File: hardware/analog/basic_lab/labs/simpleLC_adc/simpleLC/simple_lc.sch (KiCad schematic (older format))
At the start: 10 parts, among them J1 Conn_01x04_Male, Q1 FQP27P06, Q2 BC547

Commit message: Simple lc => adc v1, jlcpcb order
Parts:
- removed C2: C, Capacitor_THT:C_Axial_L12.0mm_D6.5mm_P15.00mm_Horizontal, symbol Device:C
- removed L1: L, Inductor_THT:L_Axial_L5.3mm_D2.2mm_P2.54mm_Vertical_Vishay_IM-1, symbol Device:L
- removed Q1: FQP27P06, Package_TO_SOT_THT:TO-220-3_Vertical, symbol Transistor_FET:FQP27P06
- removed R1, R2, R3: R, Resistor_THT:R_Axial_DIN0207_L6.3mm_D2.5mm_P2.54mm_Vertical, symbol Device:R
- added J2: Conn_01x02_Male, Connector_PinHeader_2.54mm:PinHeader_1x02_P2.54mm_Vertical, symbol Connector:Conn_01x02_Male
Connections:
- net labels removed: din
- wire segments 28 -> 19
- no-connect marks 0 -> 1
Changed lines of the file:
@@
 Comment4 ""
 $EndDescr
-Text GLabel 2250 2900 0    50   Input ~ 0
-din
-$Comp
-L power:+3.3V #PWR0101
-U 1 1 60C11C18
-P 3250 2000
-F 0 "#PWR0101" H 3250 1850 50  0001 C CNN
-F 1 "+3.3V" H 3265 2173 50  0000 C CNN
-F 2 "" H 3250 2000 50  0001 C CNN
-F 3 "" H 3250 2000 50  0001 C CNN
-	1    3250 2000
-	1    0    0    -1
-$EndComp
-$Comp
-L power:GND #PWR0102
-U 1 1 60C11E84
-P 3250 3650
-F 0 "#PWR0102" H 3250 3400 50  0001 C CNN
-F 1 "GND" H 3255 3477 50  0000 C CNN
-F 2 "" H 3250 3650 50  0001 C CNN
-F 3 "" H 3250 3650 50  0001 C CNN
-	1    3250 3650
-	1    0    0    -1
-$EndComp
-$Comp
-L Transistor_FET:FQP27P06 Q1
-U 1 1 60C127AE
-P 3150 2900
-F 0 "Q1" H 3354 2946 50  0000 L CNN
-F 1 "FQP27P06" H 3354 2855 50  0000 L CNN
-F 2 "Package_TO_SOT_THT:TO-220-3_Vertical" H 3350 2825 50  0001 L CIN
-F 3 "https://www.onsemi.com/pub/Collateral/FQP27P06-D.PDF" H 3150 2900 50  0001 L CNN
-	1    3150 2900
-	1    0    0    -1
-$EndComp
-$Comp
-L Device:R R1
-U 1 1 60C12EAB
-P 3250 2300
-F 0 "R1" H 3320 2346 50  0000 L CNN
-F 1 "R" H 3320 2255 50  0000 L CNN
-F 2 "Resistor_THT:R_Axial_DIN0207_L6.3mm_D2.5mm_P2.54mm_Vertical" V 3180 2300 50  0001 C CNN
-F 3 "~" H 3250 2300 50  0001 C CNN
-	1    3250 2300
-	1    0    0    -1
-$EndComp
-Wire Wire Line
-	3250 2000 3250 2150
-Wire Wire Line
-	3250 2450 3250 2550
-Wire Wire Line
-	3250 3100 3250 3200
-Wire Wire Line
-	2250 2900 2950 2900
-Wire Wire Line
-	3250 3500 3250 3650
-$Comp
-L Device:L L1
-U 1 1 60C1394D
-P 4400 2800
-F 0 "L1" H 4453 2846 50  0000 L CNN
-F 1 "L" H 4453 2755 50  0000 L CNN
-F 2 "Inductor_THT:L_Axial_L5.3mm_D2.2mm_P2.54mm_Vertical_Vishay_IM-1" H 4400 2800 50  0001 C CNN
-F 3 "~" H 4400 2800 50  0001 C CNN
-	1    4400 2800
-	1    0    0    -1
-$EndComp
-$Comp
-L power:GND #PWR0103
-U 1 1 60C13B88
-P 4400 3100
-F 0 "#PWR0103" H 4400 2850 50  0001 C CNN
-F 1 "GND" H 4405 2927 50  0000 C CNN
-F 2 "" H 4400 3100 50  0001 C CNN
-F 3 "" H 4400 3100 50  0001 C CNN
-	1    4400 3100
-	1    0    0    -1
-$EndComp
-Wire Wire Line
-	4400 2950 4400 3100
-Wire Wire Line
-	4400 2550 4400 2650
 $Comp
 L Device:C C1
@@
 	1    0    0    -1
 $EndComp
-Wire Wire Line
-	4400 2550 5100 2550
 Wire Wire Line
 	5100 2550 5100 2650
@@
 Wire Wire Line
 	5100 2950 5100 3150
-$Comp
-L Device:R R3
-U 1 1 60C14E91
-P 5650 2550
-F 0 "R3" V 5443 2550 50  0000 C CNN
-F 1 "R" V 5534 2550 50  0000 C CNN
-F 2 "Resistor_THT:R_Axial_DIN0207_L6.3mm_D2.5mm_P2.54mm_Vertical" V 5580 2550 50  0001 C CNN
-F 3 "~" H 5650 2550 50  0001 C CNN
-	1    5650 2550
-	0    1    1    0
-$EndComp
 $Comp
 L Device:R R5
@@
 Wire Wire Line
 	6300 3500 6300 3650
-Wire Wire Line
-	5100 2550 5500 2550
-Connection ~ 5100 2550
 $Comp
 L power:+3.3V #PWR0106
@@
 Wire Wire Line
 	10000 1650 10000 1450
-Text GLabel 9350 1750 2    50   Input ~ 0
-din
 Text GLabel 9350 1850 2    50   Input ~ 0
 aout
@@
 Wire Wire Line
 	6300 2850 6300 3200
-Wire Wire Line
-	5800 2550 6000 2550
 $Comp
-L Device:R R2
-U 1 1 60C12C69
-P 3250 3350
-F 0 "R2" H 3320 3396 50  0000 L CNN
-F 1 "R" H 3320 3305 50  0000 L CNN
-F 2 "Resistor_THT:R_Axial_DIN0207_L6.3mm_D2.5mm_P2.54mm_Vertical" V 3180 3350 50  0001 C CNN
-F 3 "~" H 3250 3350 50  0001 C CNN
-	1    3250 3350
+L Connector:Conn_01x02_Male J2
+U 1 1 60CB004D
+P 3850 2550
+F 0 "J2" H 3958 2731 50  0000 C CNN
+F 1 "Conn_01x02_Male" H 3958 2640 50  0000 C CNN
+F 2 "Connector_PinHeader_2.54mm:PinHeader_1x02_P2.54mm_Vertical" H 3850 2550 50  0001 C CNN
+F 3 "~" H 3850 2550 50  0001 C CNN
+	1    3850 2550
 	1    0    0    -1
 $EndComp
+Wire Wire Line
+	4050 2550 5100 2550
+Connection ~ 5100 2550
+Wire Wire Line
+	5100 2550 6000 2550
 $Comp
-L Device:C C2
-U 1 1 60C95A6B
-P 3850 2550
-F 0 "C2" V 3598 2550 50  0000 C CNN
-F 1 "C" V 3689 2550 50  0000 C CNN
-F 2 "Capacitor_THT:C_Axial_L12.0mm_D6.5mm_P15.00mm_Horizontal" H 3888 2400 50  0001 C CNN
-F 3 "~" H 3850 2550 50  0001 C CNN
-	1    3850 2550
-	0    1    1    0
+L power:GND #PWR03
+U 1 1 60CB1E67
+P 4400 3150
+F 0 "#PWR03" H 4400 2900 50  0001 C CNN
+F 1 "GND" H 4405 2977 50  0000 C CNN
+F 2 "" H 4400 3150 50  0001 C CNN
+F 3 "" H 4400 3150 50  0001 C CNN
+	1    4400 3150
+	1    0    0    -1
 $EndComp
 Wire Wire Line
-	3250 2550 3700 2550
-Connection ~ 3250 2550
+	4050 2650 4400 2650
 Wire Wire Line
-	3250 2550 3250 2700
-Wire Wire Line
-	4000 2550 4400 2550
-Connection ~ 4400 2550
+	4400 2650 4400 3150
+NoConn ~ 9350 1750
 $EndSCHEMATC

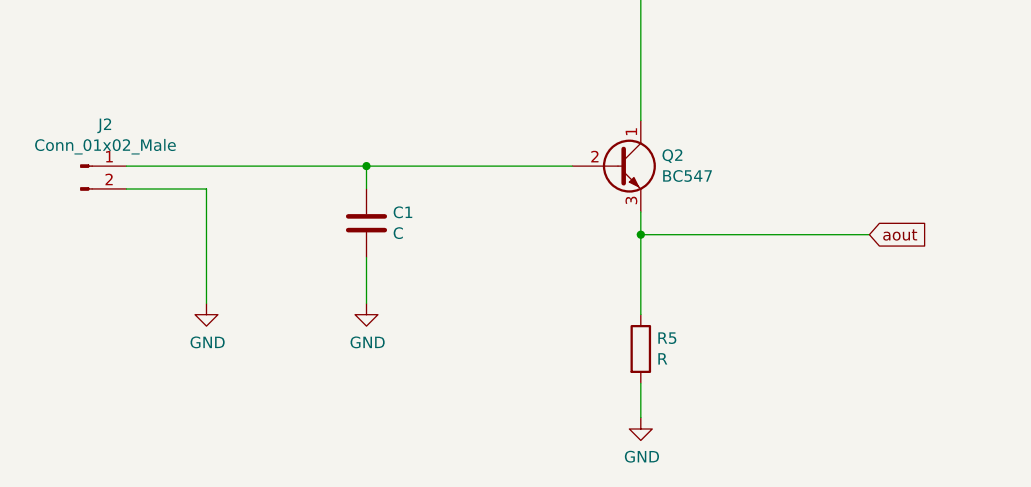
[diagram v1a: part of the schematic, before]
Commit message: pwm => adc: XFRM amplifier PCB
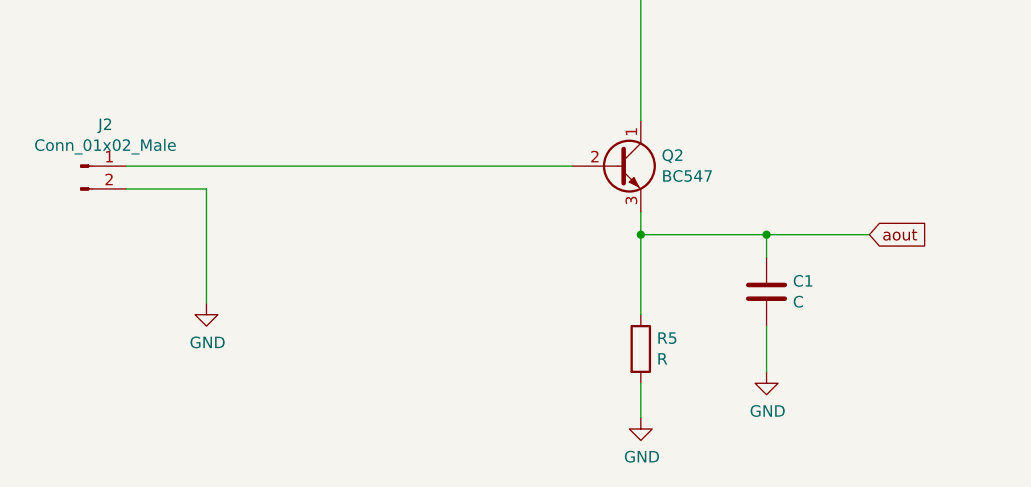
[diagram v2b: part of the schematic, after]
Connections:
- net aout: now also C1.1
- net at J2.1 (Pin_1), Q2.2 (B): no longer C1.1
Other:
- moved on the sheet: C1
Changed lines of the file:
@@
 L Device:C C1
 U 1 1 60C143B1
-P 5100 2800
-F 0 "C1" H 5215 2846 50  0000 L CNN
-F 1 "C" H 5215 2755 50  0000 L CNN
-F 2 "Capacitor_THT:C_Disc_D3.8mm_W2.6mm_P2.50mm" H 5138 2650 50  0001 C CNN
-F 3 "~" H 5100 2800 50  0001 C CNN
-	1    5100 2800
+P 6850 3100
+F 0 "C1" H 6965 3146 50  0000 L CNN
+F 1 "C" H 6965 3055 50  0000 L CNN
+F 2 "Capacitor_THT:C_Disc_D3.8mm_W2.6mm_P2.50mm" H 6888 2950 50  0001 C CNN
+F 3 "~" H 6850 3100 50  0001 C CNN
+	1    6850 3100
 	1    0    0    -1
 $EndComp
 Wire Wire Line
-	5100 2550 5100 2650
+	6850 2850 6850 2950
 $Comp
 L power:GND #PWR0104
 U 1 1 60C14856
-P 5100 3150
-F 0 "#PWR0104" H 5100 2900 50  0001 C CNN
-F 1 "GND" H 5105 2977 50  0000 C CNN
-F 2 "" H 5100 3150 50  0001 C CNN
-F 3 "" H 5100 3150 50  0001 C CNN
-	1    5100 3150
+P 6850 3450
+F 0 "#PWR0104" H 6850 3200 50  0001 C CNN
+F 1 "GND" H 6855 3277 50  0000 C CNN
+F 2 "" H 6850 3450 50  0001 C CNN
+F 3 "" H 6850 3450 50  0001 C CNN
+	1    6850 3450
 	1    0    0    -1
 $EndComp
 Wire Wire Line
-	5100 2950 5100 3150
+	6850 3250 6850 3450
 $Comp
 L Device:R R5
@@
 	6300 1650 6300 2350
 Wire Wire Line
-	6300 2850 7300 2850
+	6300 2850 6850 2850
 Connection ~ 6300 2850
 Wire Wire Line
@@
 	1    0    0    -1
 $EndComp
-Wire Wire Line
-	4050 2550 5100 2550
-Connection ~ 5100 2550
-Wire Wire Line
-	5100 2550 6000 2550
 $Comp
 L power:GND #PWR03
@@
 	4400 2650 4400 3150
 NoConn ~ 9350 1750
+Connection ~ 6850 2850
+Wire Wire Line
+	6850 2850 7300 2850
+Wire Wire Line
+	4050 2550 6000 2550
 $EndSCHEMATC

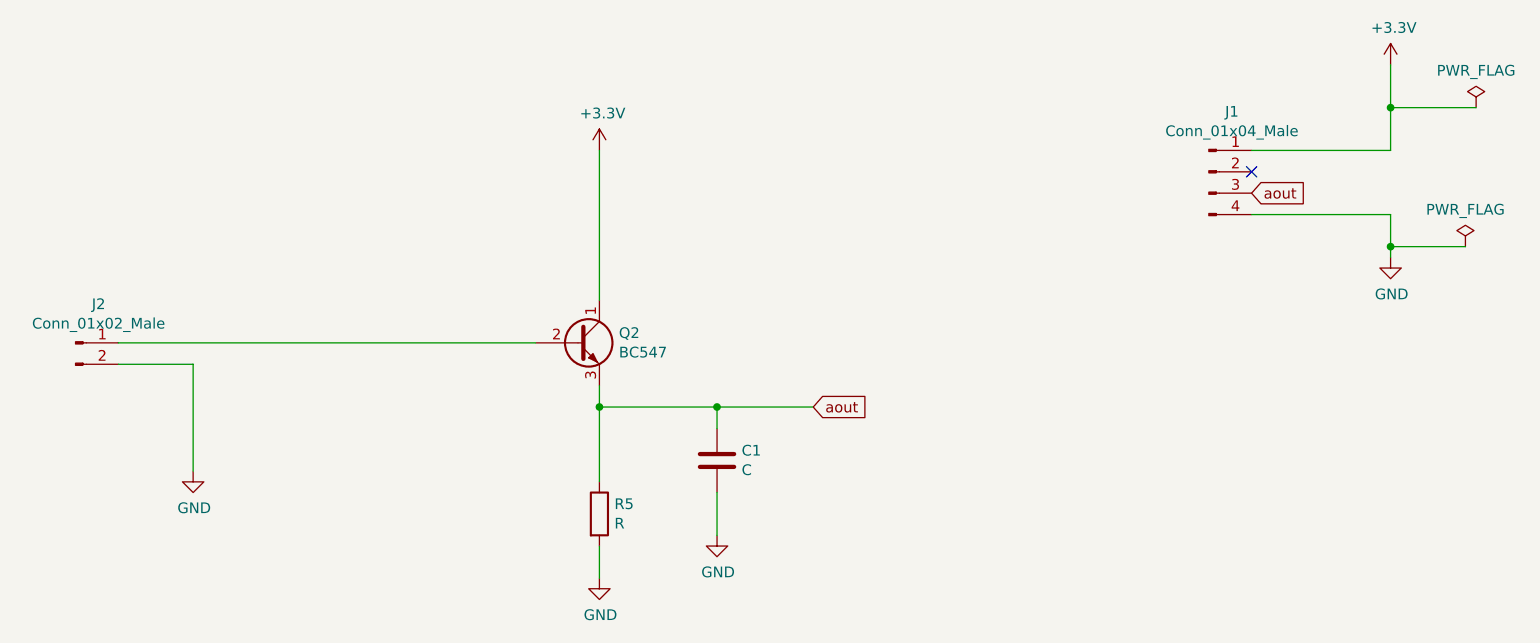
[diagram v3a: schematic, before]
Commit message: pwm => adc: started amplifier PCB
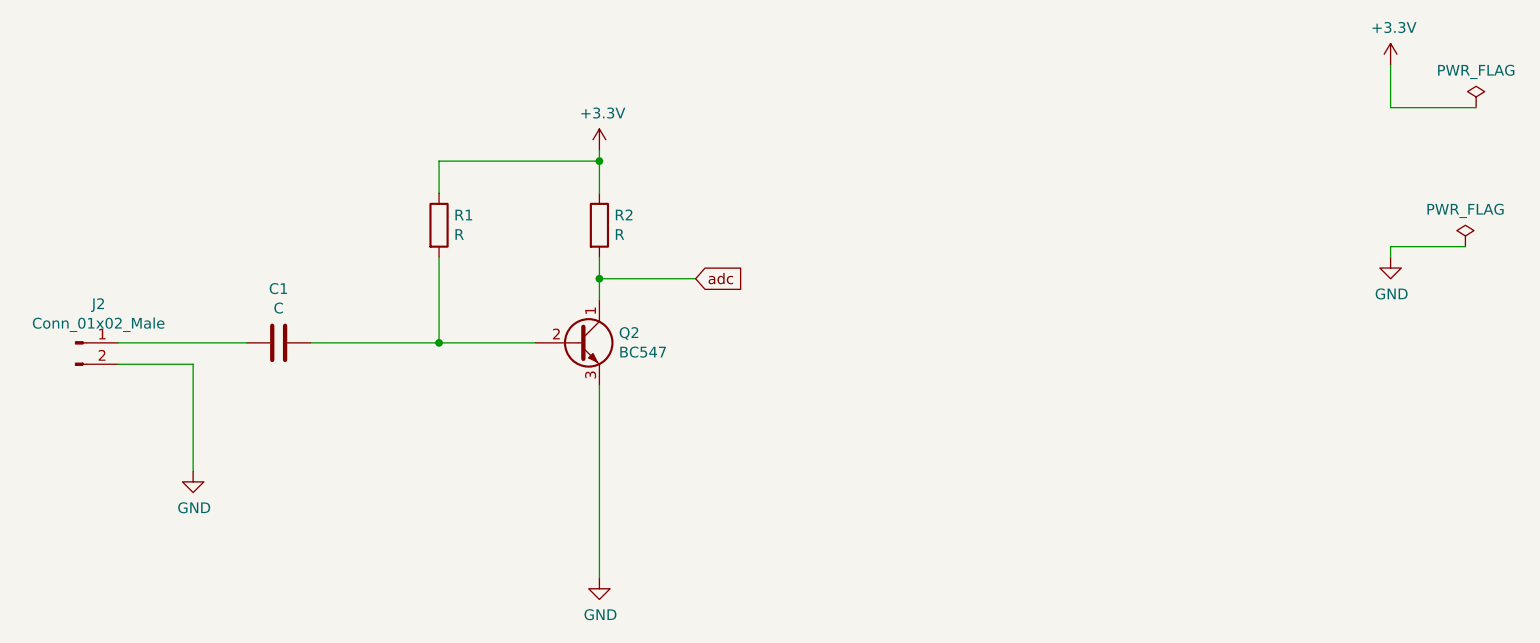
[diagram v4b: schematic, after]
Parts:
- removed J1: Conn_01x04_Male, Connector_PinHeader_2.54mm:PinHeader_1x04_P2.54mm_Vertical, symbol Connector:Conn_01x04_Male
- removed R5: R, Resistor_THT:R_Axial_DIN0207_L6.3mm_D2.5mm_P2.54mm_Vertical, symbol Device:R
- added R1, R2: R, Resistor_THT:R_Axial_DIN0309_L9.0mm_D3.2mm_P12.70mm_Horizontal, symbol Device:R
- C1: footprint Capacitor_THT:C_Disc_D3.8mm_W2.6mm_P2.50mm -> Capacitor_THT:C_Axial_L12.0mm_D6.5mm_P15.00mm_Horizontal
- Q2: footprint Package_TO_SOT_THT:TO-92_Inline -> Package_TO_SOT_THT:TO-92_Wide
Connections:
- net +3V3: now also R1.1, R2.1; no longer Q2.1 (C)
- net GND: now also Q2.3 (E); no longer C1.2
- net at Q2.2 (B): now also C1.1, R1.2; no longer J2.1 (Pin_1)
- removed net aout: C1.1, Q2.3 (E)
- new net: C1.2, J2.1 (Pin_1)
- new net adc: Q2.1 (C), R2.2
- no-connect marks 1 -> 0
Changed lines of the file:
@@
 $EndDescr
-$Comp
-L Device:C C1
-U 1 1 60C143B1
-P 6850 3100
-F 0 "C1" H 6965 3146 50  0000 L CNN
-F 1 "C" H 6965 3055 50  0000 L CNN
-F 2 "Capacitor_THT:C_Disc_D3.8mm_W2.6mm_P2.50mm" H 6888 2950 50  0001 C CNN
-F 3 "~" H 6850 3100 50  0001 C CNN
-	1    6850 3100
-	1    0    0    -1
-$EndComp
-Wire Wire Line
-	6850 2850 6850 2950
-$Comp
-L power:GND #PWR0104
-U 1 1 60C14856
-P 6850 3450
-F 0 "#PWR0104" H 6850 3200 50  0001 C CNN
-F 1 "GND" H 6855 3277 50  0000 C CNN
-F 2 "" H 6850 3450 50  0001 C CNN
-F 3 "" H 6850 3450 50  0001 C CNN
-	1    6850 3450
-	1    0    0    -1
-$EndComp
-Wire Wire Line
-	6850 3250 6850 3450
-$Comp
-L Device:R R5
-U 1 1 60C15660
-P 6300 3350
-F 0 "R5" H 6370 3396 50  0000 L CNN
-F 1 "R" H 6370 3305 50  0000 L CNN
-F 2 "Resistor_THT:R_Axial_DIN0207_L6.3mm_D2.5mm_P2.54mm_Vertical" V 6230 3350 50  0001 C CNN
-F 3 "~" H 6300 3350 50  0001 C CNN
-	1    6300 3350
-	1    0    0    -1
-$EndComp
 $Comp
 L power:GND #PWR0105
@@
 	1    0    0    -1
 $EndComp
-Wire Wire Line
-	6300 3500 6300 3650
 $Comp
 L power:+3.3V #PWR0106
@@
 F 3 "" H 6300 1650 50  0001 C CNN
 	1    6300 1650
-	1    0    0    -1
-$EndComp
-Text GLabel 7300 2850 2    50   Input ~ 0
-aout
-$Comp
-L Connector:Conn_01x04_Male J1
-U 1 1 60C2805B
-P 9150 1750
-F 0 "J1" H 9258 2031 50  0000 C CNN
-F 1 "Conn_01x04_Male" H 9258 1940 50  0000 C CNN
-F 2 "Connector_PinHeader_2.54mm:PinHeader_1x04_P2.54mm_Vertical" H 9150 1750 50  0001 C CNN
-F 3 "~" H 9150 1750 50  0001 C CNN
-	1    9150 1750
 	1    0    0    -1
 $EndComp
@@
 	1    0    0    -1
 $EndComp
-Wire Wire Line
-	9350 1950 10000 1950
-Wire Wire Line
-	10000 1950 10000 2100
-Wire Wire Line
-	9350 1650 10000 1650
-Wire Wire Line
-	10000 1650 10000 1450
-Text GLabel 9350 1850 2    50   Input ~ 0
-aout
 $Comp
 L power:PWR_FLAG #FLG02
@@
 Wire Wire Line
 	10000 2100 10350 2100
-Connection ~ 10000 2100
 Wire Wire Line
 	10000 2100 10000 2150
 Wire Wire Line
 	10000 1450 10400 1450
-Connection ~ 10000 1450
 Wire Wire Line
 	10000 1450 10000 1250
@@
 F 0 "Q2" H 6391 2596 50  0000 L CNN
 F 1 "BC547" H 6391 2505 50  0000 L CNN
-F 2 "Package_TO_SOT_THT:TO-92_Inline" H 6400 2475 50  0001 L CIN
+F 2 "Package_TO_SOT_THT:TO-92_Wide" H 6400 2475 50  0001 L CIN
 F 3 "https://www.onsemi.com/pub/Collateral/BC550-D.pdf" H 6200 2550 50  0001 L CNN
 	1    6200 2550
 	1    0    0    -1
 $EndComp
-Wire Wire Line
-	6300 2750 6300 2850
-Wire Wire Line
-	6300 1650 6300 2350
-Wire Wire Line
-	6300 2850 6850 2850
-Connection ~ 6300 2850
-Wire Wire Line
-	6300 2850 6300 3200
 $Comp
 L Connector:Conn_01x02_Male J2
@@
 Wire Wire Line
 	4400 2650 4400 3150
-NoConn ~ 9350 1750
-Connection ~ 6850 2850
 Wire Wire Line
-	6850 2850 7300 2850
+	6300 2750 6300 3650
+$Comp
+L Device:R R2
+U 1 1 60F918C5
+P 6300 2000
+F 0 "R2" H 6370 2046 50  0000 L CNN
+F 1 "R" H 6370 1955 50  0000 L CNN
+F 2 "Resistor_THT:R_Axial_DIN0309_L9.0mm_D3.2mm_P12.70mm_Horizontal" V 6230 2000 50  0001 C CNN
+F 3 "~" H 6300 2000 50  0001 C CNN
+	1    6300 2000
+	1    0    0    -1
+$EndComp
 Wire Wire Line
-	4050 2550 6000 2550
+	6300 2350 6300 2250
+Wire Wire Line
+	6300 1850 6300 1700
+$Comp
+L Device:R R1
+U 1 1 60F92B90
+P 5550 2000
+F 0 "R1" H 5620 2046 50  0000 L CNN
+F 1 "R" H 5620 1955 50  0000 L CNN
+F 2 "Resistor_THT:R_Axial_DIN0309_L9.0mm_D3.2mm_P12.70mm_Horizontal" V 5480 2000 50  0001 C CNN
+F 3 "~" H 5550 2000 50  0001 C CNN
+	1    5550 2000
+	1    0    0    -1
+$EndComp
+Wire Wire Line
+	6300 1700 5550 1700
+Wire Wire Line
+	5550 1700 5550 1850
+Connection ~ 6300 1700
+Wire Wire Line
+	6300 1700 6300 1650
+Wire Wire Line
+	5550 2150 5550 2550
+Wire Wire Line
+	5550 2550 6000 2550
+Text GLabel 6750 2250 2    50   Input ~ 0
+adc
+Wire Wire Line
+	6300 2250 6750 2250
+Connection ~ 6300 2250
+Wire Wire Line
+	6300 2250 6300 2150
+$Comp
+L Device:C C1
+U 1 1 60F96109
+P 4800 2550
+F 0 "C1" V 4548 2550 50  0000 C CNN
+F 1 "C" V 4639 2550 50  0000 C CNN
+F 2 "Capacitor_THT:C_Axial_L12.0mm_D6.5mm_P15.00mm_Horizontal" H 4838 2400 50  0001 C CNN
+F 3 "~" H 4800 2550 50  0001 C CNN
+	1    4800 2550
+	0    1    1    0
+$EndComp
+Wire Wire Line
+	4950 2550 5550 2550
+Connection ~ 5550 2550
+Wire Wire Line
+	4050 2550 4650 2550
 $EndSCHEMATC
